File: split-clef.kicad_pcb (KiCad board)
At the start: 2 copper layers, 269 x 84 mm, 31 parts, among them J3 OLED

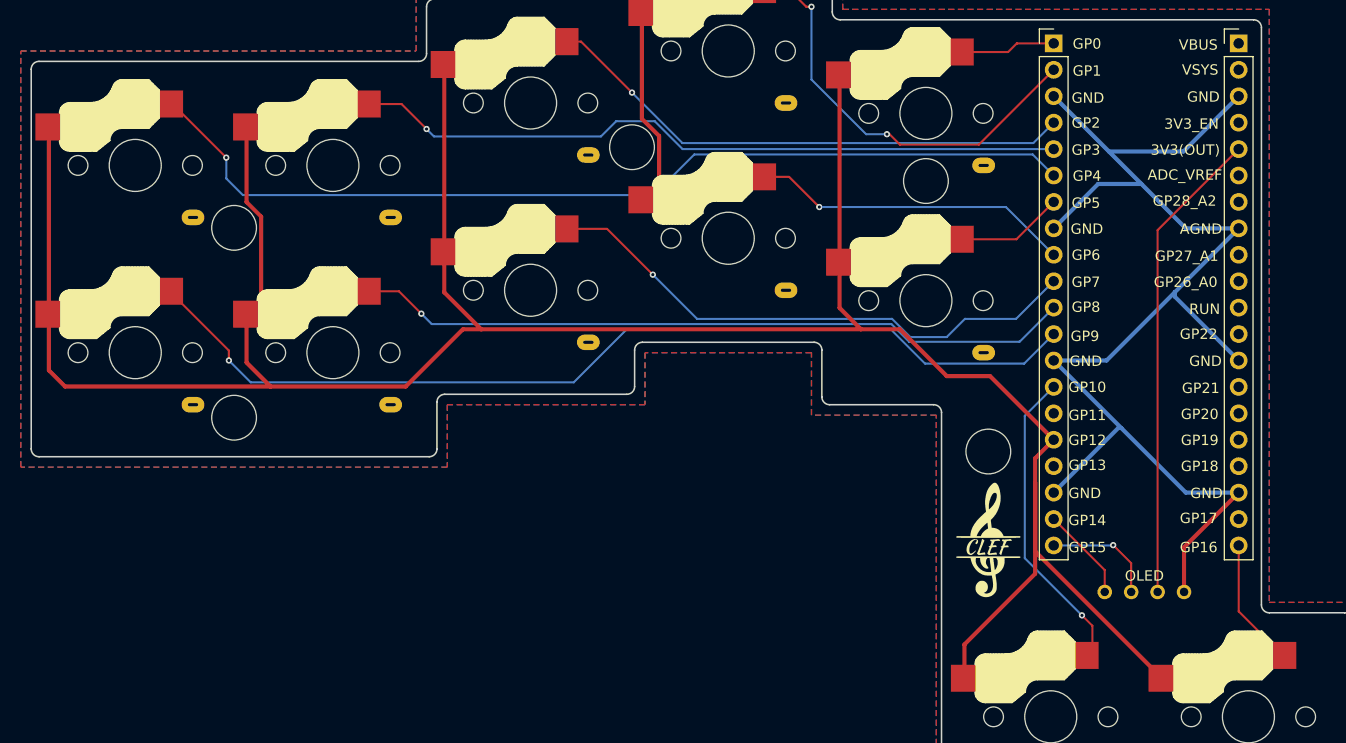
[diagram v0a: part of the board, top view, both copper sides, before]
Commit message: fixing fill zones
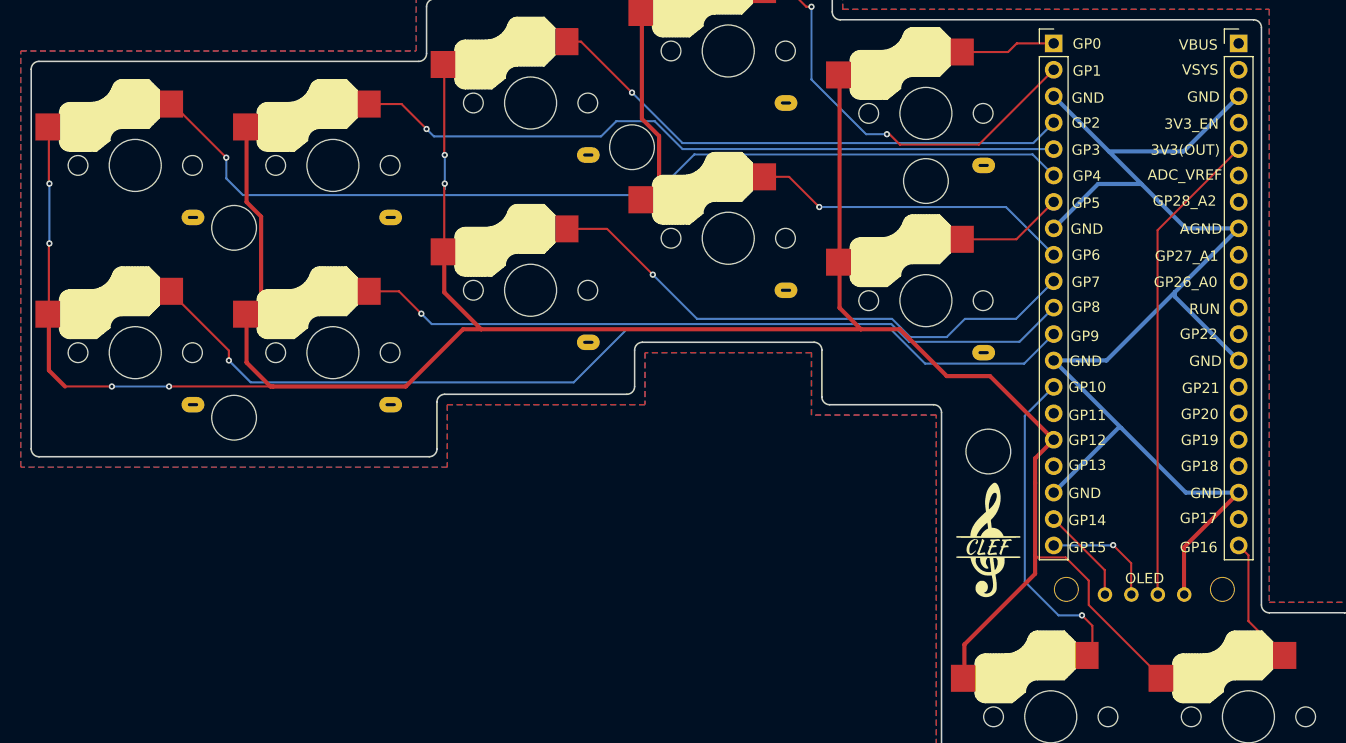
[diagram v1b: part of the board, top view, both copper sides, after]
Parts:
- J3: footprint kicad-footprints:OLED_v2 -> split-clef:1.3 Inch OLED
- moved J3 1.75 mm to (128.0, 99.8)
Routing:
- net left: track 276.4 -> 272.3 mm, vias 0 -> 6
- net LK10: track 29.9 -> 31.3 mm
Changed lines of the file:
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@@
 		(embedded_fonts no)
 	)
-	(footprint "kicad-footprints:OLED_v2"
+	(footprint "split-clef:1.3 Inch OLED"
 		(layer "F.Cu")
-		(at 128 98)
+		(at 128 99.75)
 		(descr "Connecteur 6 pins")
 		(tags "CONN DEV")
@@
 			(at 2.45 2.25 180)
 			(layer "F.Fab")
+			(hide yes)
 			(effects
 				(font
@@
 		(attr through_hole)
 		(fp_line
-			(start -6 -36.73)
-			(end 6 -36.73)
+			(start -9.5 -42)
+			(end 9.5 -42)
 			(stroke
 				(width 0.12)
@@
 		)
 		(fp_line
-			(start -6 1.27)
-			(end -6 -36.73)
+			(start -9.5 0)
+			(end -9.5 -42)
 			(stroke
 				(width 0.12)
@@
 		)
 		(fp_line
-			(start -6 1.27)
-			(end 6 1.27)
+			(start -9.5 0)
+			(end 9.5 0)
 			(stroke
 				(width 0.12)
@@
 		)
 		(fp_line
-			(start 6 -36.73)
-			(end 6 1.27)
+			(start 9.5 -42)
+			(end 9.5 0)
 			(stroke
 				(width 0.12)
@@
 		)
 		(fp_text user "OLED"
-			(at 0 -1.55 0)
+			(at 0.02 -3.05 0)
 			(layer "F.SilkS")
 			(effects
@@
 			)
 		)
+		(pad "" thru_hole circle
+			(at -7.5 -2)
+			(size 2.4 2.4)
+			(drill 2.2)
+			(layers "*.Cu" "*.Mask")
+			(remove_unused_layers no)
+		)
+		(pad "" thru_hole circle
+			(at 7.5 -2)
+			(size 2.4 2.4)
+			(drill 2.2)
+			(layers "*.Cu" "*.Mask")
+			(remove_unused_layers no)
+		)
 		(pad "1" thru_hole circle
-			(at -3.81 0)
+			(at -3.79 -1.5)
 			(size 1.397 1.397)
 			(drill 0.8128)
@@
 		)
 		(pad "2" thru_hole circle
-			(at -1.27 0)
+			(at -1.25 -1.5)
 			(size 1.397 1.397)
 			(drill 0.8128)
@@
 		)
 		(pad "3" thru_hole circle
-			(at 1.27 0)
+			(at 1.29 -1.5)
 			(size 1.397 1.397)
 			(drill 0.8128)
@@
 		)
 		(pad "4" thru_hole circle
-			(at 3.81 0)
+			(at 3.83 -1.5)
 			(size 1.397 1.397)
 			(drill 0.8128)
@@
 	)
 	(segment
+		(start 122.651 99.251)
+		(end 122.651 96.901)
+		(width 0.2)
+		(layer "F.Cu")
+		(net 16)
+	)
+	(segment
 		(start 22.7 71.3)
 		(end 22.7 76.7)
@@
 	)
 	(segment
-		(start 117.5 94.1)
-		(end 117.5 87.5)
-		(width 0.4)
+		(start 117.681 94.681)
+		(end 117.5 94.5)
+		(width 0.2)
+		(layer "F.Cu")
+		(net 16)
+	)
+	(segment
+		(start 60.7 55.95)
+		(end 60.75 56)
+		(width 0.2)
 		(layer "F.Cu")
 		(net 16)
@@
 	)
 	(segment
-		(start 22.7 53.3)
-		(end 22.7 71.3)
-		(width 0.4)
+		(start 60.7 58.8)
+		(end 60.7 65.3)
+		(width 0.2)
 		(layer "F.Cu")
 		(net 16)
@@
 	)
 	(segment
+		(start 60.75 58.75)
+		(end 60.7 58.8)
+		(width 0.2)
+		(layer "F.Cu")
+		(net 16)
+	)
+	(segment
+		(start 120.431 94.681)
+		(end 117.681 94.681)
+		(width 0.2)
+		(layer "F.Cu")
+		(net 16)
+	)
+	(segment
 		(start 41.7 75.95)
 		(end 44 78.25)
@@
 	)
 	(segment
-		(start 129.7 106.3)
-		(end 117.5 94.1)
-		(width 0.4)
+		(start 22.7 64.55)
+		(end 22.7 71.3)
+		(width 0.2)
 		(layer "F.Cu")
 		(net 16)
@@
 	)
 	(segment
+		(start 22.75 64.5)
+		(end 22.7 64.55)
+		(width 0.2)
+		(layer "F.Cu")
+		(net 16)
+	)
+	(segment
+		(start 60.7 47.3)
+		(end 60.7 55.95)
+		(width 0.2)
+		(layer "F.Cu")
+		(net 16)
+	)
+	(segment
+		(start 22.7 53.3)
+		(end 22.7 58.7)
+		(width 0.2)
+		(layer "F.Cu")
+		(net 16)
+	)
+	(segment
+		(start 22.7 58.7)
+		(end 22.75 58.75)
+		(width 0.2)
+		(layer "F.Cu")
+		(net 16)
+	)
+	(segment
 		(start 79.7 52.521631)
 		(end 81.351 54.172631)
@@
 	)
 	(segment
+		(start 34.25 78.25)
+		(end 44.25 78.25)
+		(width 0.2)
+		(layer "F.Cu")
+		(net 16)
+	)
+	(segment
 		(start 98.7 66.3)
 		(end 98.7 70.7)
@@
 	(segment
 		(start 117.5 96.25)
-		(end 117.5 87.5)
+		(end 117.5 94.5)
 		(width 0.4)
 		(layer "F.Cu")
@@
 	)
 	(segment
+		(start 122.651 96.901)
+		(end 120.431 94.681)
+		(width 0.2)
+		(layer "F.Cu")
+		(net 16)
+	)
+	(segment
 		(start 79.7 42.3)
 		(end 79.7 52.521631)
@@
 	)
 	(segment
+		(start 44 78.25)
+		(end 44.25 78.25)
+		(width 0.4)
+		(layer "F.Cu")
+		(net 16)
+	)
+	(segment
+		(start 117.5 94.5)
+		(end 117.5 87.5)
+		(width 0.4)
+		(layer "F.Cu")
+		(net 16)
+	)
+	(segment
 		(start 41.7 71.3)
 		(end 41.7 75.95)
@@
 	(segment
 		(start 24.25 78.25)
-		(end 44 78.25)
-		(width 0.4)
+		(end 28.75 78.25)
+		(width 0.2)
 		(layer "F.Cu")
 		(net 16)
@@
 	)
 	(segment
-		(start 44 78.25)
+		(start 44.25 78.25)
 		(end 57 78.25)
 		(width 0.4)
@@
 	)
 	(segment
+		(start 129.7 106.3)
+		(end 122.651 99.251)
+		(width 0.2)
+		(layer "F.Cu")
+		(net 16)
+	)
+	(segment
 		(start 41.7 60.521631)
 		(end 43.101 61.922631)
@@
 		(net 16)
 	)
+	(via
+		(at 22.75 58.75)
+		(size 0.6)
+		(drill 0.3)
+		(layers "F.Cu" "B.Cu")
+		(net 16)
+	)
+	(via
+		(at 22.75 64.5)
+		(size 0.6)
+		(drill 0.3)
+		(layers "F.Cu" "B.Cu")
+		(net 16)
+	)
+	(via
+		(at 28.75 78.25)
+		(size 0.6)
+		(drill 0.3)
+		(layers "F.Cu" "B.Cu")
+		(net 16)
+	)
+	(via
+		(at 60.75 56)
+		(size 0.6)
+		(drill 0.3)
+		(layers "F.Cu" "B.Cu")
+		(net 16)
+	)
+	(via
+		(at 60.75 58.75)
+		(size 0.6)
+		(drill 0.3)
+		(layers "F.Cu" "B.Cu")
+		(net 16)
+	)
+	(via
+		(at 34.25 78.25)
+		(size 0.6)
+		(drill 0.3)
+		(layers "F.Cu" "B.Cu")
+		(net 16)
+	)
 	(segment
-		(start 60.7 47.3)
-		(end 60.7 65.3)
-		(width 0.4)
-		(layer "F.Cu")
+		(start 60.75 59.25)
+		(end 60.75 58.75)
+		(width 0.2)
+		(layer "B.Cu")
+		(net 16)
+	)
+	(segment
+		(start 22.75 58.75)
+		(end 22.75 64.5)
+		(width 0.2)
+		(layer "B.Cu")
+		(net 16)
+	)
+	(segment
+		(start 28.75 78.25)
+		(end 34.25 78.25)
+		(width 0.2)
+		(layer "B.Cu")
+		(net 16)
+	)
+	(segment
+		(start 60.75 56)
+		(end 60.75 59.25)
+		(width 0.2)
+		(layer "B.Cu")
 		(net 16)
 	)
@@
 	)
 	(segment
-		(start 116.5 81.0725)
-		(end 119.2825 78.29)
+		(start 119.75 100.25)
+		(end 116.5 97)
 		(width 0.2)
 		(layer "B.Cu")
@@
 	)
 	(segment
-		(start 122 100.25)
-		(end 116.5 94.75)
+		(start 116.5 97)
+		(end 116.5 81.0725)
 		(width 0.2)
 		(layer "B.Cu")
@@
 	)
 	(segment
-		(start 116.5 94.75)
-		(end 116.5 81.0725)
+		(start 116.5 81.0725)
+		(end 119.2825 78.29)
+		(width 0.2)
+		(layer "B.Cu")
+		(net 26)
+	)
+	(segment
+		(start 122 100.25)
+		(end 119.75 100.25)
 		(width 0.2)
 		(layer "B.Cu")
@@
 	(segment
 		(start 141.3 104.1)
-		(end 137.0625 99.8625)
+		(end 138 100.8)
 		(width 0.2)
 		(layer "F.Cu")
@@
 	)
 	(segment
-		(start 137.0625 99.8625)
+		(start 138 94.4675)
 		(end 137.0625 93.53)
 		(width 0.2)
@@
 	)
 	(segment
+		(start 138 100.8)
+		(end 138 94.4675)
+		(width 0.2)
+		(layer "F.Cu")
+		(net 27)
+	)
+	(segment
 		(start 34.3 69.1)
 		(end 40 74.8)
@@
 			(thermal_gap 0.5)
 			(thermal_bridge_width 0.5)
-			(island_removal_mode 1)
+			(island_removal_mode 2)
 			(island_area_min 10)
 		)

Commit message: first iteration done
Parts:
- removed the J3 at (128.0, 99.8)
- removed the REF** at (117.5, 43.5)
- removed the Ref** at (113.0, 84.5)
- added J3: OLED, kicad-footprints:OLED_v2, F.Cu at (240.4, 136.3)
- added J3: OLED, kicad-footprints:OLED_v2, F.Cu at (185.9, 136.3)
- added JET: JST_PH_S2B-PH-K_1x02_P2.00mm_Horizontal, Connector_JST:JST_PH_S2B-PH-K_1x02_P2.00mm_Horizontal, B.Cu at (255.1, 154.2)
- added JET: JST_PH_S2B-PH-K_1x02_P2.00mm_Horizontal, Connector_JST:JST_PH_S2B-PH-K_1x02_P2.00mm_Horizontal, B.Cu at (171.3, 152.6)
- added LOGO: LOGO, split-clef:logo, F.Cu at (235.9, 144.9)
- added MCU: SuperMini, split-clef:SuperMini NRF52840, F.Cu at (178.0, 101.5)
- added MCU: SuperMini, split-clef:SuperMini NRF52840, F.Cu at (233.0, 101.5)
- added REF**: Breakaway_Tabs, kicad-footprints:Breakaway_Tabs, F.Cu at (298.7, 97.5)
- added REF**: Breakaway_Tabs, kicad-footprints:Breakaway_Tabs, F.Cu at (99.6, 142.0)
- added REF**: Breakaway_Tabs, kicad-footprints:Breakaway_Tabs, F.Cu at (238.7, 176.9)
- added REF**: Breakaway_Tabs, kicad-footprints:Breakaway_Tabs, F.Cu at (128.1, 97.6)
- added REF**: Adafruit QSPI DIP Breakout Board, split-clef:Adafruit QSPI DIP Breakout Board, F.Cu at (168.7, 137.6)
- added REF**: Breakaway_Tabs, kicad-footprints:Breakaway_Tabs, F.Cu at (326.7, 142.0)
- added REF**: Adafruit QSPI DIP Breakout Board, split-clef:Adafruit QSPI DIP Breakout Board, F.Cu at (247.8, 137.0)
- added REF**: Breakaway_Tabs, kicad-footprints:Breakaway_Tabs, F.Cu at (187.6, 177.0)
- added REF**: Breakaway_Tabs, kicad-footprints:Breakaway_Tabs, F.Cu at (166.2, 99.6)
- added REF**: Breakaway_Tabs, kicad-footprints:Breakaway_Tabs, F.Cu at (260.2, 99.5)
- added RS3: , kicad-footprints:ChocV1_V2_Hotswap, B.Cu at (336.2, 131.8)
- added RS3: , kicad-footprints:ChocV1_V2_Hotswap, B.Cu at (336.2, 113.8)
- added RSW1: SW_PUSH, kicad-footprints:ResetSW_1side, F.Cu at (235.8, 153.1)
- added RSW1: SW_PUSH, kicad-footprints:ResetSW_1side, F.Cu at (190.5, 153.0)
- moved LOGO 92.9 mm to (190.4, 144.5)
- moved H4 81.9 mm to (99.6, 138.1)
- moved LS5 81.9 mm to (90.1, 131.8)
- moved LS6 81.9 mm to (109.1, 131.8)
- moved H1 81.9 mm to (187.6, 172.3)
- moved H3 81.9 mm to (99.6, 119.8)
- moved LS0 81.9 mm to (90.1, 113.8)
- moved LS1 81.9 mm to (109.1, 113.8)
- moved LS10 81.9 mm to (178.1, 166.8)
- moved LS11 81.9 mm to (197.1, 166.8)
- moved LS2 81.9 mm to (128.1, 107.8)
- moved LS3 81.9 mm to (147.1, 102.8)
- moved LS4 81.9 mm to (166.1, 108.8)
- moved LS7 81.9 mm to (128.1, 125.8)
- moved LS8 81.9 mm to (147.1, 120.8)
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- renumbered Ref** to H1, Ref** to H2, Ref** to H3, Ref** to H4, G*** to LOGO, S2 to LS0, S2 to LS1, S9 to LS10, S10 to LS11, S4 to LS2, S6 to LS3, S8 to LS4, S2 to LS5, S1 to LS6, S3 to LS7, S5 to LS8, S7 to LS9, S18 to RS0, S16 to RS1, S14 to RS2, S12 to RS3, S17 to RS4, S15 to RS5, S13 to RS6, S11 to RS7, S20 to RS8, S19 to RS9
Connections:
- RS0 pad 1: GND -> right
- RS0 pad 2: P10 -> RK0
- RS1 pad 1: GND -> right
- RS1 pad 2: P14 -> RK1
- RS2 pad 1: GND -> right
- RS2 pad 2: P18 -> RK2
- RS3 pad 1: GND -> right
- RS3 pad 2: P20 -> RK3
- RS4 pad : (no net) -> right
- RS4 pad 2: P26 -> RK5
- RS5 pad 1: GND -> right
- RS5 pad 2: P15 -> RK6
- RS6 pad 1: GND -> right
- RS6 pad 2: P19 -> RK7
- RS7 pad 1: GND -> right
- RS7 pad 2: P21 -> RK8
- RS8 pad 1: GND -> right
- RS8 pad 2: P9 -> RK10
- RS9 pad 1: GND -> right
- RS9 pad 2: P8 -> RK11
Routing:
- net right: track 0.00 -> 266.6 mm, vias 0 -> 2
- net RK4: track 0.00 -> 145.2 mm
- net R-GND: track 0.00 -> 136.5 mm, vias 0 -> 24
- net RK3: track 0.00 -> 130.3 mm
- net RK9: track 0.00 -> 123.2 mm
- net RK2: track 0.00 -> 114.5 mm
- net RK8: track 0.00 -> 104.3 mm
- net RK7: track 0.00 -> 89.6 mm
- net R-Raw: track 0.00 -> 68.4 mm
- net RAW: track 0.00 -> 58.5 mm, vias 0 -> 5
- net LK11: track 12.3 -> 62.5 mm, vias 0 -> 1
- net RST: track 0.00 -> 47.8 mm
- net R-RST: track 0.00 -> 47.2 mm, vias 0 -> 2
- net RK1: track 0.00 -> 46.3 mm, vias 0 -> 1
- net left: track 272.3 -> 316.3 mm, vias 6 -> 0
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- added copper zone on B.Cu, net R-GND
- added copper zone on F.Cu, net R-GND
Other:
- board size 269 x 84 mm -> 267.2 x 106.8 mm
- board text added: "+"
- board text added: "GND"

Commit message: jlcpcb
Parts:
- added M2_Mount: , kicad-footprints:M2_HOLE_v2, F.Cu at (326.7, 138.2)
- added M2_Mount: , kicad-footprints:M2_HOLE_v2, F.Cu at (269.8, 112.0)
- added M2_Mount: , kicad-footprints:M2_HOLE_v2, F.Cu at (326.8, 119.2)
- added M2_Mount: , kicad-footprints:M2_HOLE_v2, F.Cu at (238.7, 171.9)
- added Ref**: Val**, kicad-footprints:M2_HOLE_v2, F.Cu at (288.6, 111.8)
- LS0, LS1, LS10, LS11, LS2, LS3, LS4, LS5, LS6, LS7, LS8, LS9, RS0, RS1, RS2, RS3 (x3), RS4, RS5, RS6, RS7, RS8, RS9: moved to F.Cu
- moved H2 5.78 mm to (156.6, 111.8)
- moved Ref** 0.24 mm to (137.8, 111.8)
- turned LS0 to 180 degrees
- turned LS1 to 180 degrees
- turned LS10 to 180 degrees
- turned LS11 to 180 degrees
- turned LS2 to 180 degrees
- turned LS3 to 180 degrees
- turned LS4 to 180 degrees
- turned LS5 to 180 degrees
- turned LS6 to 180 degrees
- turned LS7 to 180 degrees
- turned LS8 to 180 degrees
- turned LS9 to 180 degrees
- turned RS0 to 180 degrees
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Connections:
- MCU pad 13: RK0 -> RK1
- MCU pad 14: RK1 -> RK0
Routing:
- net left: track 316.3 -> 0.00 mm
- net RK4: track 145.2 -> 0.00 mm
- net R-GND: track 136.5 -> 0.00 mm, vias 24 -> 0
- net RK3: track 130.3 -> 0.00 mm
- net RK9: track 123.2 -> 0.00 mm
- net LK5: track 117.5 -> 0.00 mm
- net GND: track 117.2 -> 0.00 mm, vias 26 -> 0
- net RK2: track 114.5 -> 0.00 mm
- net RK8: track 104.3 -> 0.00 mm
- net LK0: track 99.4 -> 0.00 mm, vias 1 -> 0
- net RK7: track 89.6 -> 0.00 mm
- net LK6: track 89.1 -> 0.00 mm
- net LK1: track 73.2 -> 0.00 mm, vias 1 -> 0
- net R-Raw: track 68.4 -> 0.00 mm
- net right: track 266.6 -> 199.9 mm, vias 2 -> 0
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
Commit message: v1.0
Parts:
- moved REF** 0.83 mm to (246.9, 137.0)
- moved JET 0.21 mm to (254.9, 154.3)
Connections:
- MCU pad 10: RK4 -> RK9
- MCU pad 5: RK7 -> RK2
- MCU pad 6: RK2 -> RK7
- MCU pad 7: RK8 -> RK3
- MCU pad 8: RK3 -> RK8
- MCU pad 9: RK9 -> RK4
- RS4 pad : right -> (no net)
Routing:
- net left: track 0.00 -> 312.2 mm
- net RK4: track 0.00 -> 131.0 mm
- net R-GND: track 0.00 -> 130.6 mm, vias 0 -> 28
- net LK5: track 0.00 -> 120.0 mm, vias 0 -> 1
- net GND: track 0.00 -> 113.3 mm, vias 0 -> 23
- net RK9: track 0.00 -> 113.2 mm
- net RK3: track 0.00 -> 108.9 mm
- net LK0: track 0.00 -> 104.8 mm, vias 0 -> 1
- net RK2: track 0.00 -> 95.0 mm
- net LK6: track 0.00 -> 93.4 mm, vias 0 -> 1
- net RK8: track 0.00 -> 93.2 mm
- net LK1: track 0.00 -> 86.6 mm, vias 0 -> 1
- net RK7: track 0.00 -> 80.1 mm
- net R-Raw: track 0.00 -> 73.9 mm, vias 0 -> 2
- net LK2: track 0.00 -> 69.9 mm, vias 0 -> 1
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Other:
- outline, holes or cut-outs redrawn
